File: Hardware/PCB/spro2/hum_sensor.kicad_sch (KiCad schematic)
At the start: 22 parts, among them IC1 TL074CN, U5 ${SIM.PARAMS}, U6 ${SIM.PARAMS}, U7 ${SIM.PARAMS}

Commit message: Updated schematic and 1st version of the PCB
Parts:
- removed D1, D2, D3, D4: D, symbol Device:D
- removed IC1: TL074CN, DIP794W53P254L1930H508Q14N, symbol TL074CN:TL074CN
- removed RSensor: 47k, symbol Device:R
- removed U5, U6, U7: ${SIM.PARAMS}, symbol Simulation_SPICE:OPAMP
- added D1, D2, D3, D4: 1N4148, Diode_THT:D_DO-35_SOD27_P7.62mm_Horizontal, symbol Diode:1N4148
- added J3: Humidity sensor, Diplomna:connector_2p, symbol Connector:Screw_Terminal_01x02
- added U3: TL074, SPRO_lib:DIP794W53P254L1930H508Q14N, symbol Amplifier_Operational:TL074
- C4: renamed from C3; footprint (none) -> Capacitor_THT:CP_Radial_D5.0mm_P2.00mm
- C5: renamed from C4; footprint (none) -> Capacitor_THT:CP_Radial_D5.0mm_P2.00mm
- R10: renamed from R9; footprint (none) -> Resistor_THT:R_Axial_DIN0207_L6.3mm_D2.5mm_P10.16mm_Horizontal
- R11: renamed from R10; footprint (none) -> Resistor_THT:R_Axial_DIN0207_L6.3mm_D2.5mm_P10.16mm_Horizontal
- R12: renamed from R11; footprint (none) -> Resistor_THT:R_Axial_DIN0207_L6.3mm_D2.5mm_P10.16mm_Horizontal
- R13, R14, R17, R18, R19: footprint (none) -> Resistor_THT:R_Axial_DIN0207_L6.3mm_D2.5mm_P10.16mm_Horizontal
- R15: renamed from R16; footprint (none) -> Resistor_THT:R_Axial_DIN0207_L6.3mm_D2.5mm_P10.16mm_Horizontal
- R16: renamed from R15; footprint (none) -> Resistor_THT:R_Axial_DIN0207_L6.3mm_D2.5mm_P10.16mm_Horizontal
- R9: renamed from R8; footprint (none) -> Resistor_THT:R_Axial_DIN0207_L6.3mm_D2.5mm_P10.16mm_Horizontal
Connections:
- net +5V: now also U3.4 (V+)
- net GND: now also U3.6 (-), U3.9 (-)
- net Humidity_Out: now also U3.8
- net at R15.2, R17.2, R18.1: now also U3.10 (+)
- net at C4.1, C5.1, R10.2: now also U3.2 (-)
- net at R11.1, R9.2: now also D1.2 (A), D2.1 (K), U3.3 (+)
- net at R11.2, R12.2: now also D1.1 (K), D2.2 (A), J3.1 (Pin_1), U3.1
- net at R13.1, R14.1, R15.1: now also J3.2 (Pin_2)
- net at R16.2, R17.1: now also D4.2 (A)
- net at R14.2, R16.1: now also D3.1 (K), U3.5 (+)
- new net: D3.2 (A), D4.1 (K), U3.7
- new net -5V: U3.11 (V-)

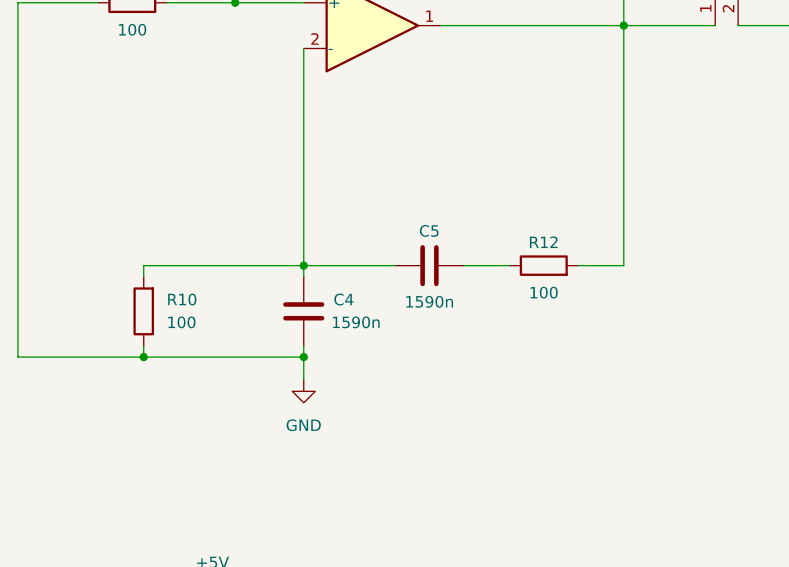
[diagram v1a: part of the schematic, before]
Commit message: Updated circuit
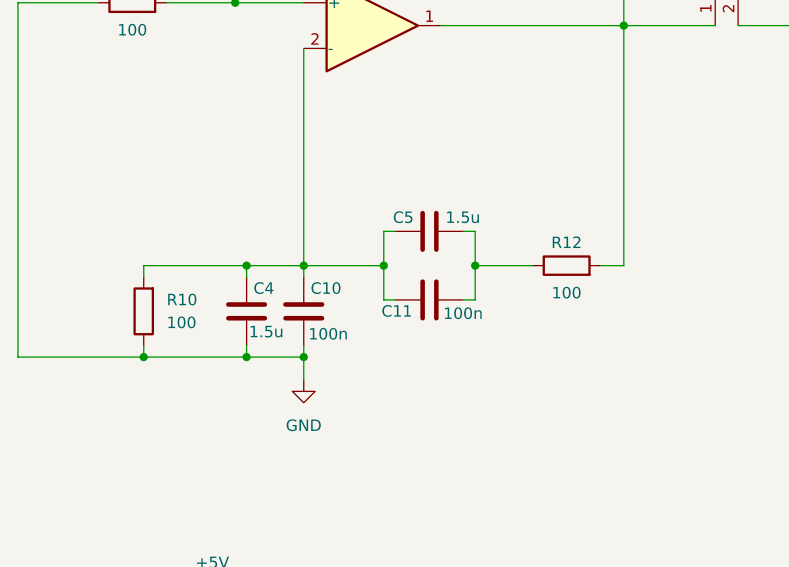
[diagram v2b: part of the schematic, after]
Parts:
- added C10, C11: 100n, C_Rect_L7.2mm_W3.0mm_P5.00mm_FKS2_FKP2_MKS2_MKP2, symbol Device:C
- C4, C5: value 1590n -> 1.5u; footprint Capacitor_THT:CP_Radial_D5.0mm_P2.00mm -> C_Rect_L7.2mm_W8.5mm_P5.00mm_FKP2_FKP2_MKS2_MKP2
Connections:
- net GND: now also C10.2
- net at C4.1, R10.2, U3.2 (-): now also C5.2, C10.1, C11.2; no longer C5.1
- net at R12.1: now also C5.1, C11.1; no longer C5.2
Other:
- moved on the sheet: C4, R12

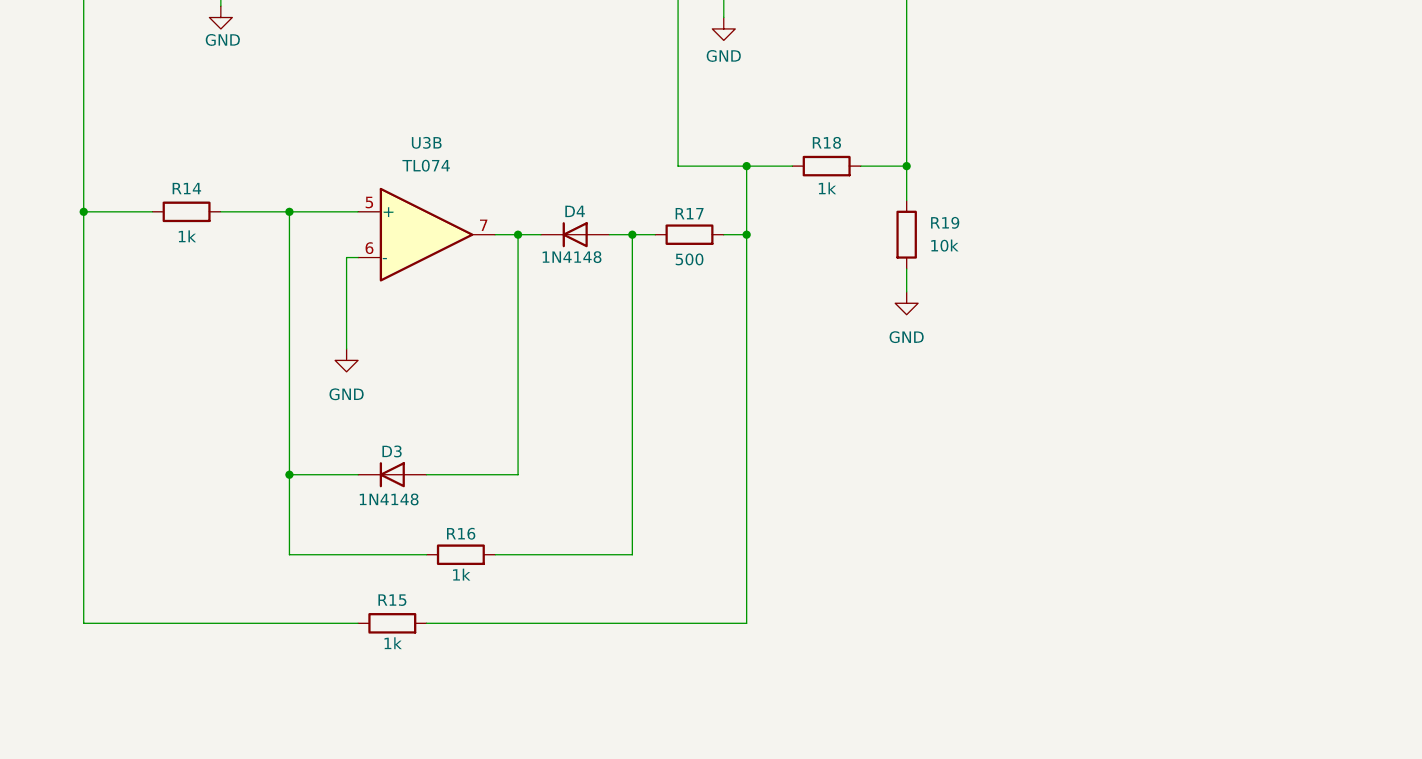
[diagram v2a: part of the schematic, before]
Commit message: Changes to humidity circuit. Add MAX660 circuit
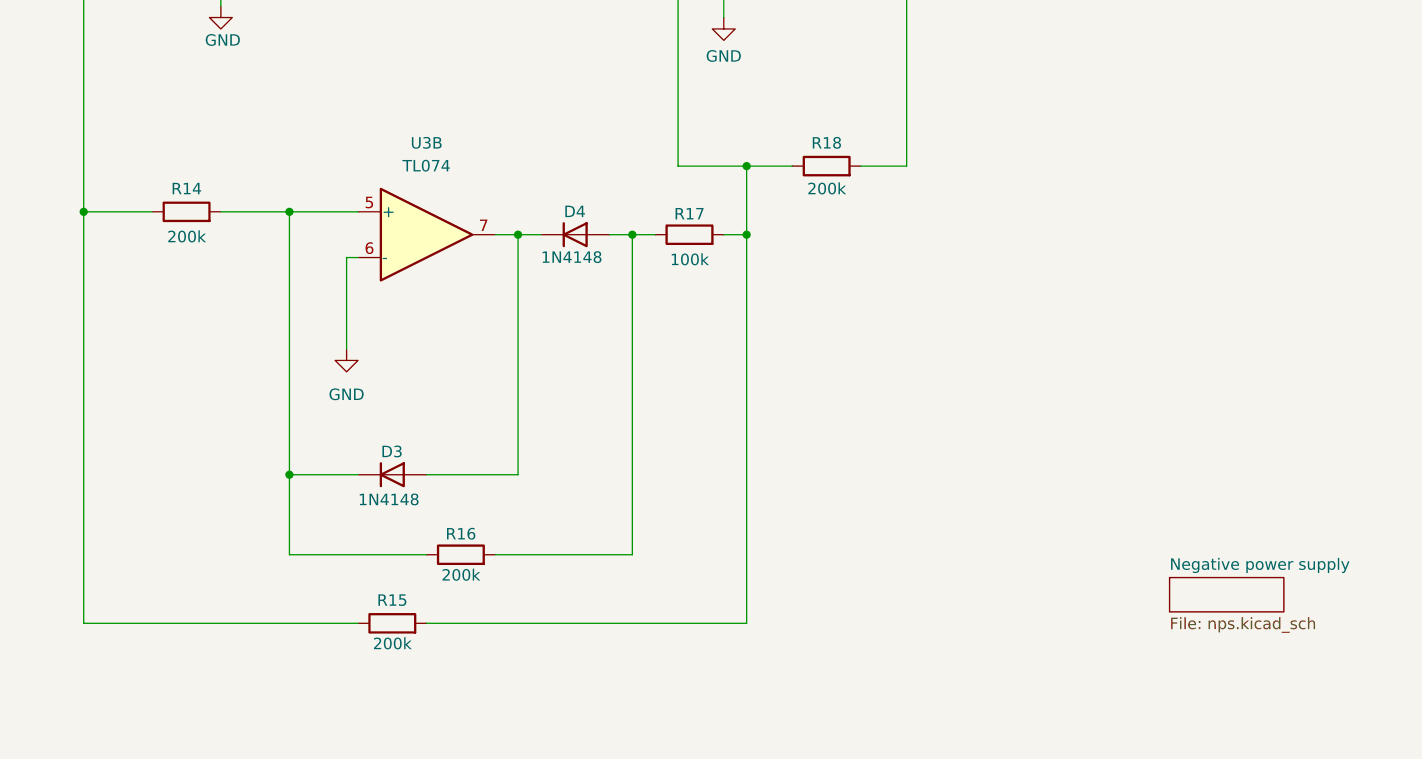
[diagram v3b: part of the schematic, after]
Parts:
- removed R19: 10k, Resistor_THT:R_Axial_DIN0207_L6.3mm_D2.5mm_P10.16mm_Horizontal, symbol Device:R
- R14, R15, R16, R18: value 1k -> 200k
- R17: value 500 -> 100k
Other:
- added sheet Negative power supply (nps.kicad_sch)
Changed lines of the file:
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@@
-	)
-	(junction
-		(at 233.68 101.6)
-		(diameter 0)
-		(color 0 0 0 0)
 	)
 	(junction
@@
 	(wire
 		(pts
-			(xy 233.68 101.6) (xy 233.68 105.41)
-		)
-		(stroke
-			(width 0)
-			(type default)
-		)
-	)
-	(wire
-		(pts
 			(xy 66.04 105.41) (xy 66.04 106.68)
 		)
@@
 		(pts
 			(xy 157.48 78.74) (xy 153.67 78.74)
-		)
-		(stroke
-			(width 0)
-			(type default)
-		)
-	)
-	(wire
-		(pts
-			(xy 233.68 113.03) (xy 233.68 115.57)
 		)
 		(stroke
@@
 	)
 	(symbol
-		(lib_id "power:GND")
-		(at 233.68 115.57 0)
-		(unit 1)
-		(exclude_from_sim no)
-		(in_bom yes)
-		(on_board yes)
-		(dnp no)
-		(fields_autoplaced yes)
-		(property "Reference" "#PWR025"
-			(at 233.68 121.92 0)
-			(effects
-				(font
-					(size 1.27 1.27)
-				)
-				(hide yes)
-			)
-		)
-		(property "Value" "GND"
-			(at 233.68 120.65 0)
-			(effects
-				(font
-					(size 1.27 1.27)
-				)
-			)
-		)
-		(property "Footprint" ""
-			(at 233.68 115.57 0)
-			(effects
-				(font
-					(size 1.27 1.27)
-				)
-				(hide yes)
-			)
-		)
-		(property "Datasheet" ""
-			(at 233.68 115.57 0)
-			(effects
-				(font
-					(size 1.27 1.27)
-				)
-				(hide yes)
-			)
-		)
-		(property "Description" "Power symbol creates a global label with name \"GND\" , ground"
-			(at 233.68 115.57 0)
-			(effects
-				(font
-					(size 1.27 1.27)
-				)
-				(hide yes)
-			)
-		)
-		(pin "1"
-		)
-		(instances
-			(project "spro2"
-				(path "/edfea366-2226-45cc-893f-1155e0ffe333/64df08b9-4000-4721-b83a-705bd7162f6e"
-					(reference "#PWR025")
-					(unit 1)
-				)
-			)
-		)
-	)
-	(symbol
 		(lib_id "power:+5V")
 		(at 73.66 142.24 0)
@@
 			)
 		)
-		(property "Value" "500"
+		(property "Value" "100k"
 			(at 209.55 112.014 90)
 			(effects
@@
 			)
 		)
-		(property "Value" "1k"
+		(property "Value" "200k"
 			(at 153.67 109.474 90)
 			(effects
@@
 			)
 		)
-		(property "Value" "1k"
+		(property "Value" "200k"
 			(at 224.79 104.14 90)
 			(effects
@@
 			)
 		)
-		(property "Value" "1k"
+		(property "Value" "200k"
 			(at 184.15 147.066 90)
 			(effects
@@
 			)
 		)
-		(property "Value" "1k"
+		(property "Value" "200k"
 			(at 176.53 154.686 90)
 			(effects
@@
 	)
 	(symbol
-		(lib_id "Device:R")
-		(at 233.68 109.22 0)
-		(unit 1)
-		(exclude_from_sim no)
-		(in_bom yes)
-		(on_board yes)
-		(dnp no)
-		(fields_autoplaced yes)
-		(property "Reference" "R19"
-			(at 236.22 107.9499 0)
-			(effects
-				(font
-					(size 1.27 1.27)
-				)
-				(justify left)
-			)
-		)
-		(property "Value" "10k"
-			(at 236.22 110.4899 0)
-			(effects
-				(font
-					(size 1.27 1.27)
-				)
-				(justify left)
-			)
-		)
-		(property "Footprint" "Resistor_THT:R_Axial_DIN0207_L6.3mm_D2.5mm_P10.16mm_Horizontal"
-			(at 231.902 109.22 90)
-			(effects
-				(font
-					(size 1.27 1.27)
-				)
-				(hide yes)
-			)
-		)
-		(property "Datasheet" "~"
-			(at 233.68 109.22 0)
-			(effects
-				(font
-					(size 1.27 1.27)
-				)
-				(hide yes)
-			)
-		)
-		(property "Description" "Resistor"
-			(at 233.68 109.22 0)
-			(effects
-				(font
-					(size 1.27 1.27)
-				)
-				(hide yes)
-			)
-		)
-		(pin "1"
-		)
-		(pin "2"
-		)
-		(instances
-			(project "spro2"
-				(path "/edfea366-2226-45cc-893f-1155e0ffe333/64df08b9-4000-4721-b83a-705bd7162f6e"
-					(reference "R19")
-					(unit 1)
-				)
-			)
-		)
-	)
-	(symbol
 		(lib_id "Device:C")
 		(at 77.47 110.49 0)
@@
 				)
 			)
+		)
+	)
+	(sheet
+		(at 262.89 147.32)
+		(size 12.7 3.81)
+		(fields_autoplaced yes)
+		(stroke
+			(width 0.1524)
+			(type solid)
+		)
+		(fill
+			(color 0 0 0 0.0000)
+		)
+		(property "Sheetname" "Negative power supply"
+			(at 262.89 146.6084 0)
+			(effects
+				(font
+					(size 1.27 1.27)
+				)
+				(justify left bottom)
+			)
+		)
+		(property "Sheetfile" "nps.kicad_sch"
+			(at 262.89 151.7146 0)
+			(effects
+				(font
+					(size 1.27 1.27)
+				)
+				(justify left top)
+			)
+		)
+		(instances
+			(project "spro2"
+				(path "/edfea366-2226-45cc-893f-1155e0ffe333/64df08b9-4000-4721-b83a-705bd7162f6e"
+					(page "5")
+				)
+			)
